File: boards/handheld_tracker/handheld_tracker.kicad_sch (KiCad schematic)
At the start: 15 parts, among them U1 SAM-M8Q, U2 RFM96W-433S2, U4 LM3670MF

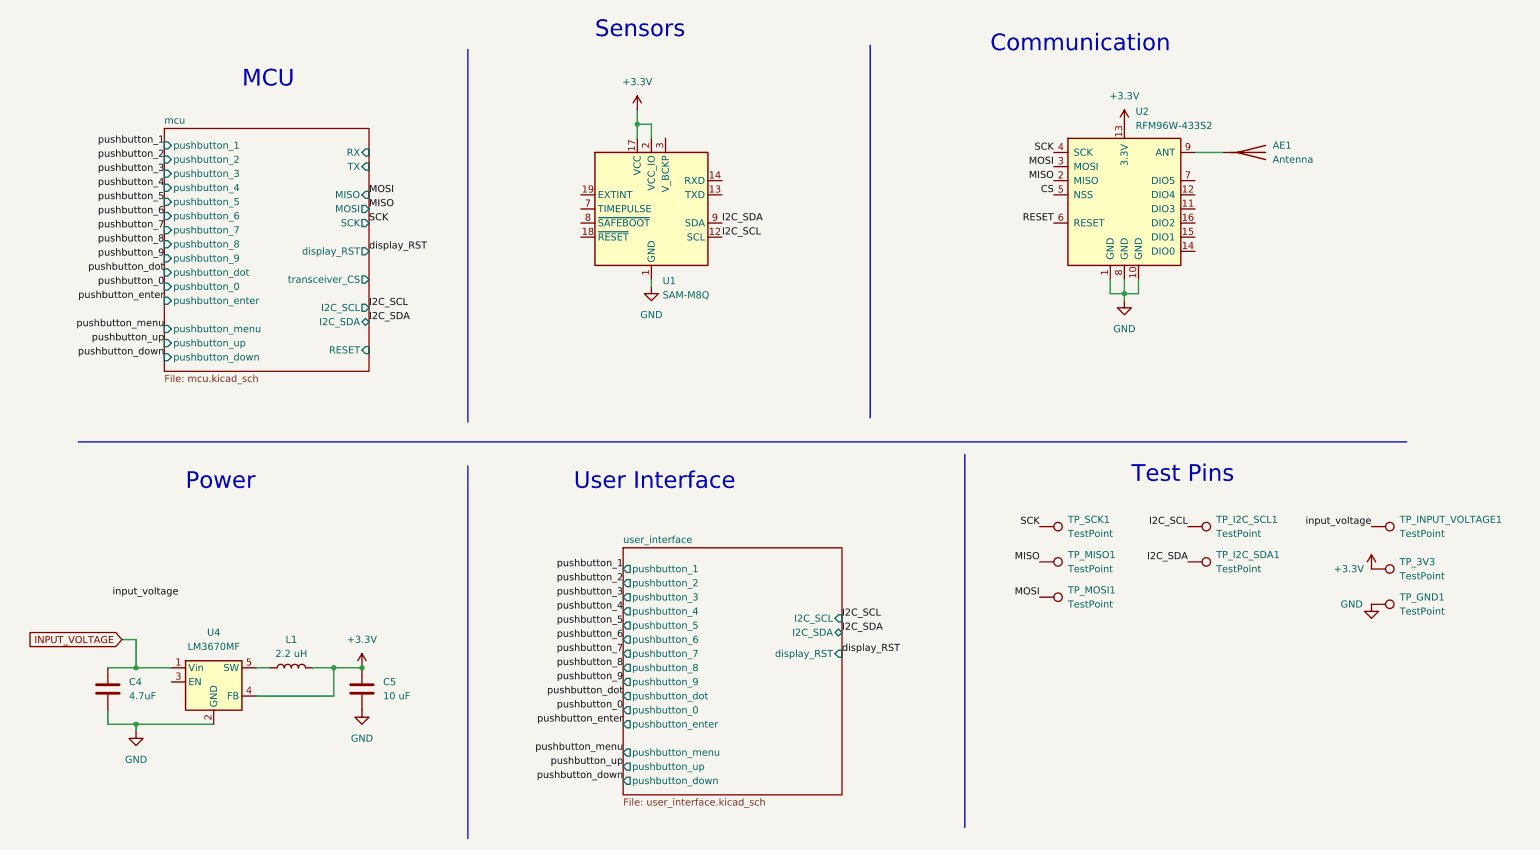
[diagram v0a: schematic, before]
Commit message: added traces for buttons
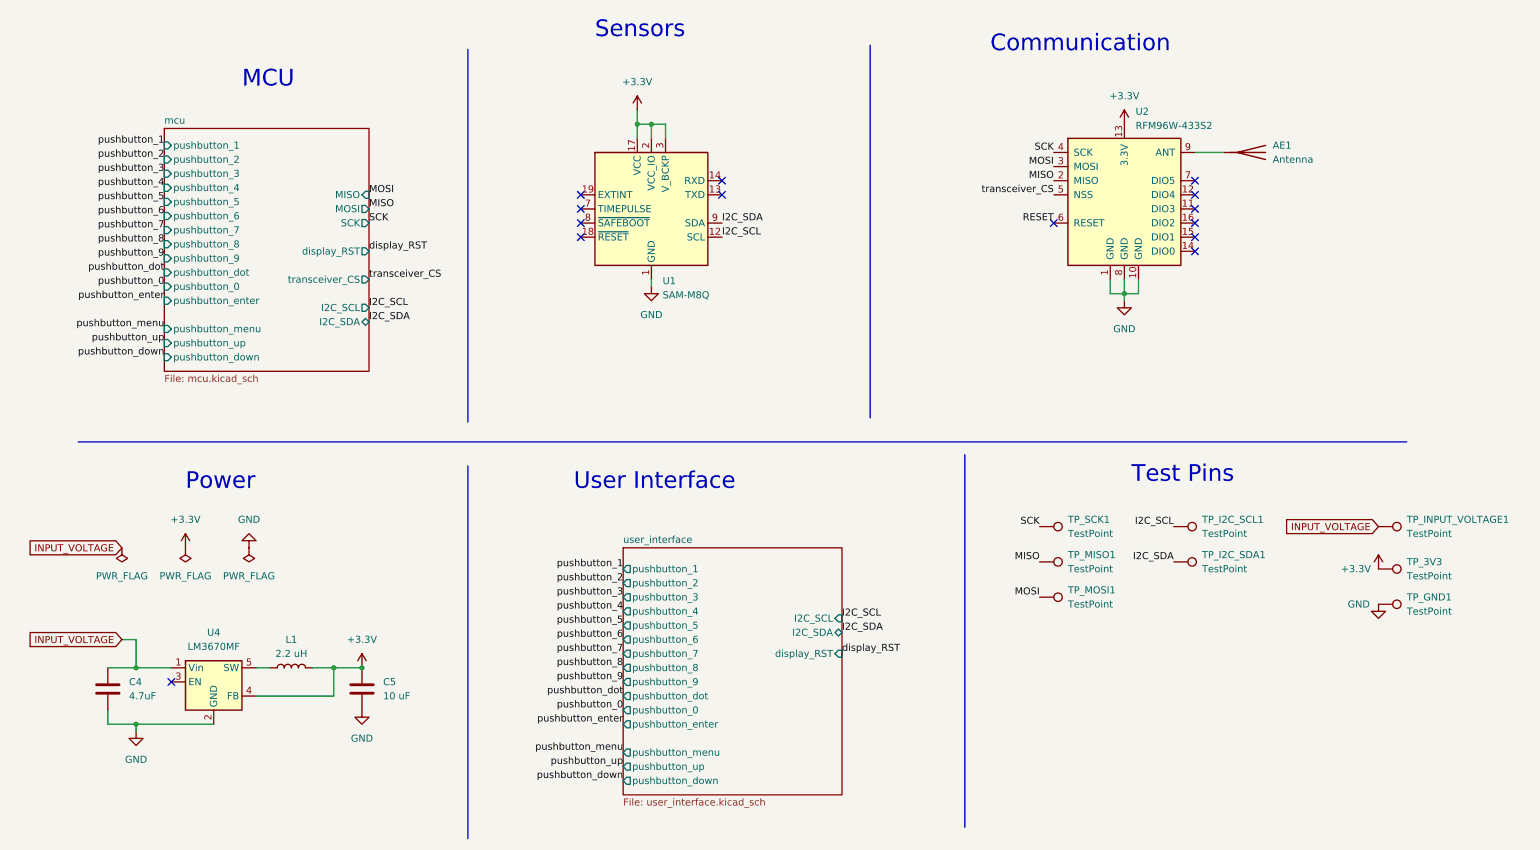
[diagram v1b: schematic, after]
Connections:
- net input_voltage is gone; now on net INPUT_VOLTAGE: TP_INPUT_VOLTAGE1.1
- net +3.3V: now also U1.3 (V_BCKP)
- net CS renamed transceiver_CS
- no-connect marks 0 -> 14
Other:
- sheet mcu ports: added none; removed RESET, RX, TX
- moved on the sheet: TP_3V3, TP_GND1, TP_I2C_SCL1, TP_I2C_SDA1, TP_INPUT_VOLTAGE1

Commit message: changed push buttons' 3v to ground, added conn component to power supply
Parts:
- added J3: Conn_01x02_Pin, Connector_PinHeader_2.54mm:PinHeader_1x02_P2.54mm_Vertical, symbol Connector:Conn_01x02_Pin
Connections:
- net GND: now also J3.2 (Pin_2)
- net INPUT_VOLTAGE: now also J3.1 (Pin_1)
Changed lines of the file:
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@@
 	(paper "A4")
+	(junction
+		(at 55.88 115.57)
+		(diameter 0)
+		(color 0 0 0 0)
+	)
 	(junction
 		(at 128.27 39.37)
@@
 	(wire
 		(pts
+			(xy 74.93 113.03) (xy 74.93 115.57)
+		)
+		(stroke
+			(width 0)
+			(type default)
+		)
+	)
+	(wire
+		(pts
 			(xy 213.36 67.31) (xy 213.36 69.85)
 		)
@@
 	(wire
 		(pts
+			(xy 74.93 110.49) (xy 74.93 100.33)
+		)
+		(stroke
+			(width 0)
+			(type default)
+		)
+	)
+	(wire
+		(pts
 			(xy 130.81 39.37) (xy 128.27 39.37)
 		)
@@
 	(wire
 		(pts
+			(xy 74.93 115.57) (xy 55.88 115.57)
+		)
+		(stroke
+			(width 0)
+			(type default)
+		)
+	)
+	(wire
+		(pts
 			(xy 71.12 137.16) (xy 71.12 142.24)
 		)
@@
 	(wire
 		(pts
+			(xy 33.02 115.57) (xy 35.56 115.57)
+		)
+		(stroke
+			(width 0)
+			(type default)
+		)
+	)
+	(wire
+		(pts
 			(xy 210.82 67.31) (xy 210.82 69.85)
 		)
@@
 	(wire
 		(pts
+			(xy 35.56 100.33) (xy 35.56 115.57)
+		)
+		(stroke
+			(width 0)
+			(type default)
+		)
+	)
+	(wire
+		(pts
 			(xy 67.31 137.16) (xy 71.12 137.16)
+		)
+		(stroke
+			(width 0)
+			(type default)
+		)
+	)
+	(wire
+		(pts
+			(xy 74.93 100.33) (xy 35.56 100.33)
 		)
 		(stroke
@@
 					(unit 1)
 				)
+			)
+		)
+	)
+	(symbol
+		(lib_id "Connector:Conn_01x02_Pin")
+		(at 69.85 110.49 0)
+		(unit 1)
+		(exclude_from_sim no)
+		(in_bom yes)
+		(on_board yes)
+		(dnp no)
+		(fields_autoplaced yes)
+		(property "Reference" "J3"
+			(at 70.485 105.41 0)
+			(effects
+				(font
+					(size 1.27 1.27)
+				)
+			)
+		)
+		(property "Value" "Conn_01x02_Pin"
+			(at 70.485 107.95 0)
+			(effects
+				(font
+					(size 1.27 1.27)
+				)
+			)
+		)
+		(property "Footprint" "Connector_PinHeader_2.54mm:PinHeader_1x02_P2.54mm_Vertical"
+			(at 69.85 110.49 0)
+			(effects
+				(font
+					(size 1.27 1.27)
+				)
+				(hide yes)
+			)
+		)
+		(property "Datasheet" "~"
+			(at 69.85 110.49 0)
+			(effects
+				(font
+					(size 1.27 1.27)
+				)
+				(hide yes)
+			)
+		)
+		(property "Description" "Generic connector, single row, 01x02, script generated"
+			(at 69.85 110.49 0)
+			(effects
+				(font
+					(size 1.27 1.27)
+				)
+				(hide yes)
+			)
+		)
+		(pin "1"
+		)
+		(pin "2"
+		)
+		(instances
+			(project "handheld_tracker"
+				(path "/0d71301b-e65e-49f8-81f9-e7516dc11624"
+					(reference "J3")
+					(unit 1)
+				)

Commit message: finished board pre-review
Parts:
- removed TP_3V3, TP_GND1, TP_I2C_SCL1, TP_I2C_SDA1, TP_INPUT_VOLTAGE1, TP_MISO1, TP_MOSI1, TP_SCK1: TestPoint, TestPoint:TestPoint_Pad_D3.0mm, symbol Connector:TestPoint
- added J4: Conn_01x05_Pin, Connector_PinHeader_2.54mm:PinHeader_1x05_P2.54mm_Vertical, symbol Connector:Conn_01x05_Pin
- added J5: Conn_01x03_Pin, Connector_PinHeader_2.54mm:PinHeader_1x03_P2.54mm_Vertical, symbol Connector:Conn_01x03_Pin
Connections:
- net +3.3V: now also J5.2 (Pin_2)
- net GND: now also J5.3 (Pin_3)
- net I2C_SCL: now also J4.4 (Pin_4)
- net I2C_SDA: now also J4.5 (Pin_5)
- net INPUT_VOLTAGE: now also J5.1 (Pin_1)
- net MISO: now also J4.1 (Pin_1)
- net MOSI: now also J4.2 (Pin_2)
- net SCK: now also J4.3 (Pin_3)
